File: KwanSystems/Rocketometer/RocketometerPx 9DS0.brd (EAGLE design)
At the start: 55.9 x 22.9 mm, 55 parts, among them J001 USB_MICROB_JSTGCT, J102 JST 2mm, J401 M07, J501 GP-2106, J701 MICROSD-SOCKET, Q501 SSM6N58NU, Q502 SSM6N58NU, U001 FT232RLSSOP, U101 MCP73831, U201 1.8/3.3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

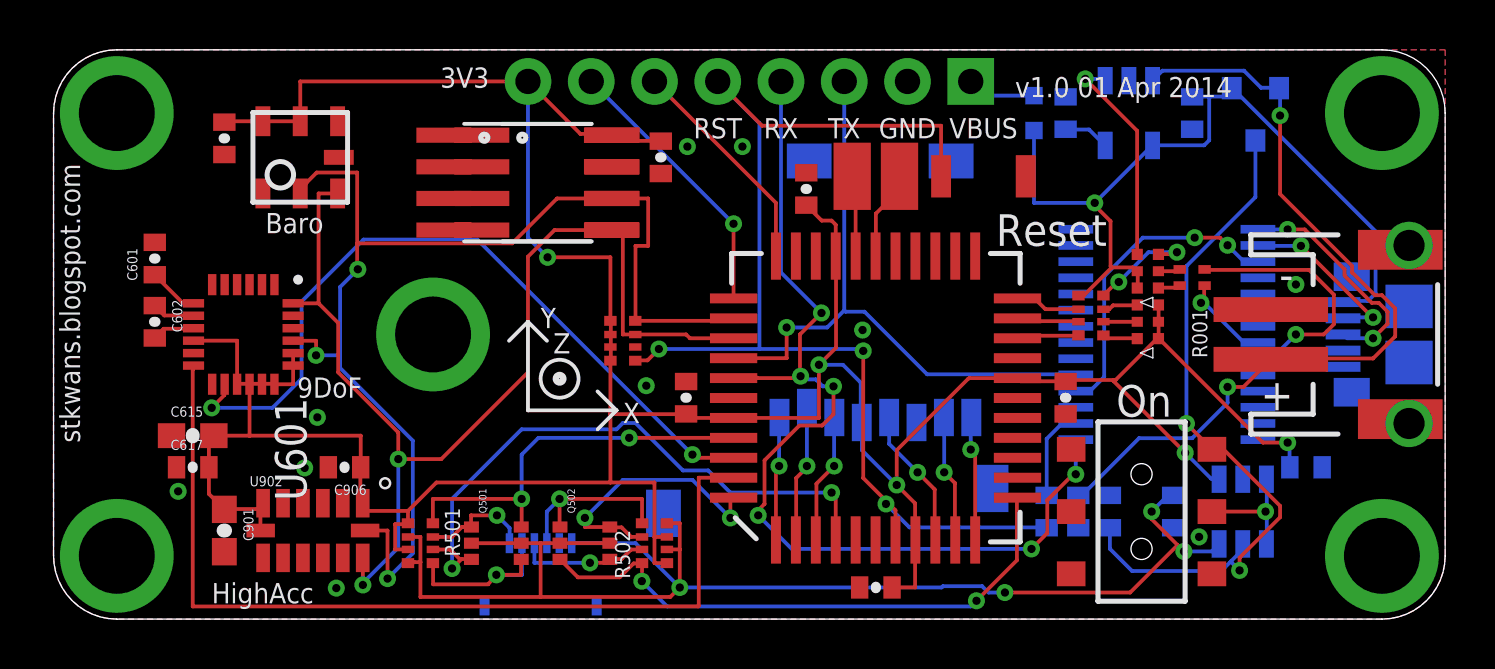
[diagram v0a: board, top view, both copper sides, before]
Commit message: More work on pure vector XR2 skin
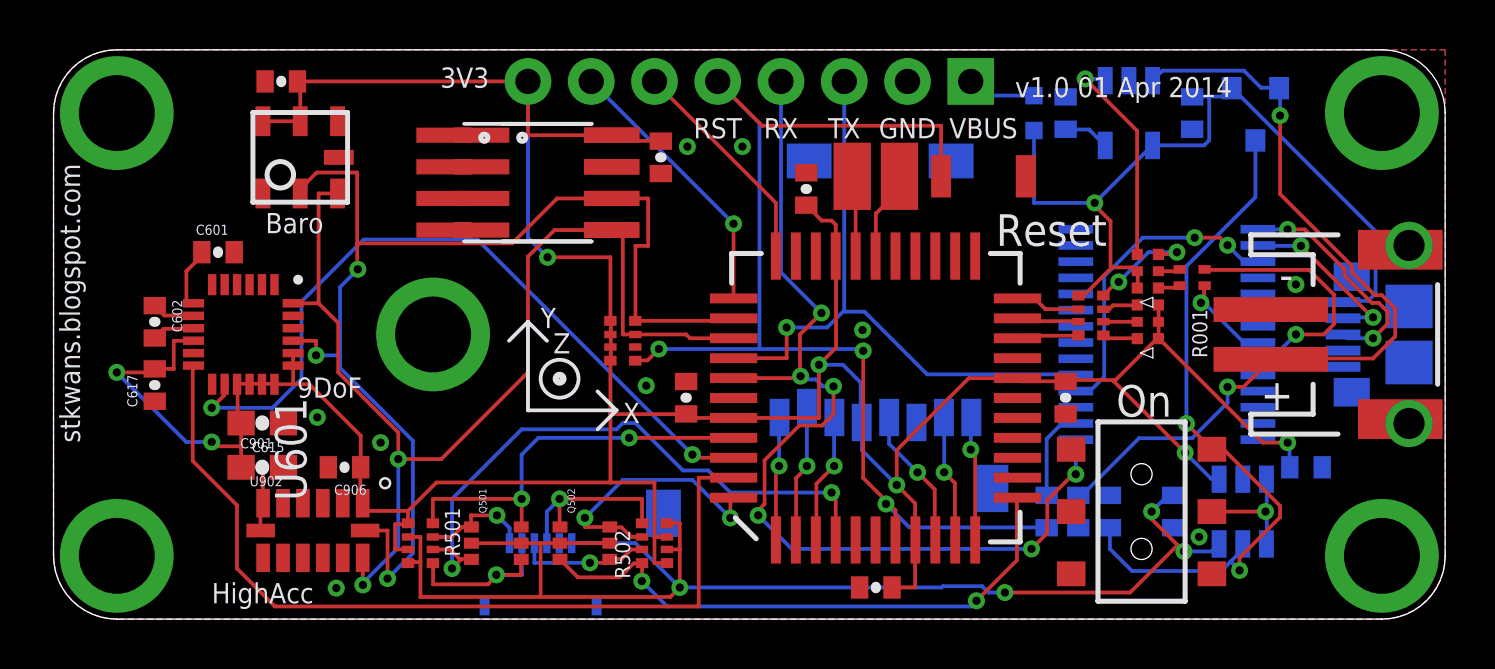
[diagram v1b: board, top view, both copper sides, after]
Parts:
- moved C617 3.64 mm to (4.06, 9.40), turned to 90 degrees
- moved C101 3.23 mm to (9.14, 21.6), turned to 180 degrees
- moved C901 2.96 mm to (8.38, 6.10), turned to 0 degrees
- moved C615 2.84 mm to (8.38, 7.87), turned to 180 degrees
- moved C601 2.55 mm to (6.60, 14.7), turned to 0 degrees
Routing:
- net VCC: track 142.4 -> 145.5 mm, vias 5 -> 7
- net GYROINT: track 36.6 -> 34.6 mm
- net N$3: track 2.04 -> 2.62 mm

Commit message: Shuffled several documents
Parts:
- J001: value USB_MICROB_JSTGCT -> USB_MICROB_JSTFCI; device KwanSystems:USB_MICROB_3075 -> KwanSystems:USB-MICROB-CONN-09505
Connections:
- net GND: now also J001.P1, J001.P2, J001.P3, J001.P4, J001.P5, J001.P6; no longer J001.P$1, J001.P$10, J001.P$2, J001.P$3, J001.P$4, J001.P$8
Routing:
- net 1.8V: track 56.1 -> 64.2 mm, vias 4 -> 3
- net VBUS: track 36.6 -> 33.1 mm, vias 1 -> 3
- net VLIPO: track 33.3 -> 30.0 mm, vias 2 -> 1
- net VCC: track 145.5 -> 142.6 mm
- net VIN: track 28.5 -> 26.8 mm, vias 2 -> 3
- net TXLED1: track 10.4 -> 9.04 mm, vias 1 -> 3
- net D-: track 7.05 -> 7.54 mm, vias 2 -> 0
- net D+: track 9.31 -> 8.96 mm, vias 2 -> 0
